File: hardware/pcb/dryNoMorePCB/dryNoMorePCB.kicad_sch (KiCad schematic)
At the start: 25 parts, among them J1 USB_A_Stacked, J10 Jack-DC, J11 Conn_01x03, J2 Conn_01x03, J3 Conn_01x03, J4 Conn_01x03, J5 USB_A_Stacked, J6 Conn_01x03, J7 Conn_01x03, J8 Conn_01x03, J9 USB_A_Stacked, M1 MNMOS, M2 MNMOS, M3 MNMOS, M4 MNMOS, M5 MNMOS, M6 MNMOS

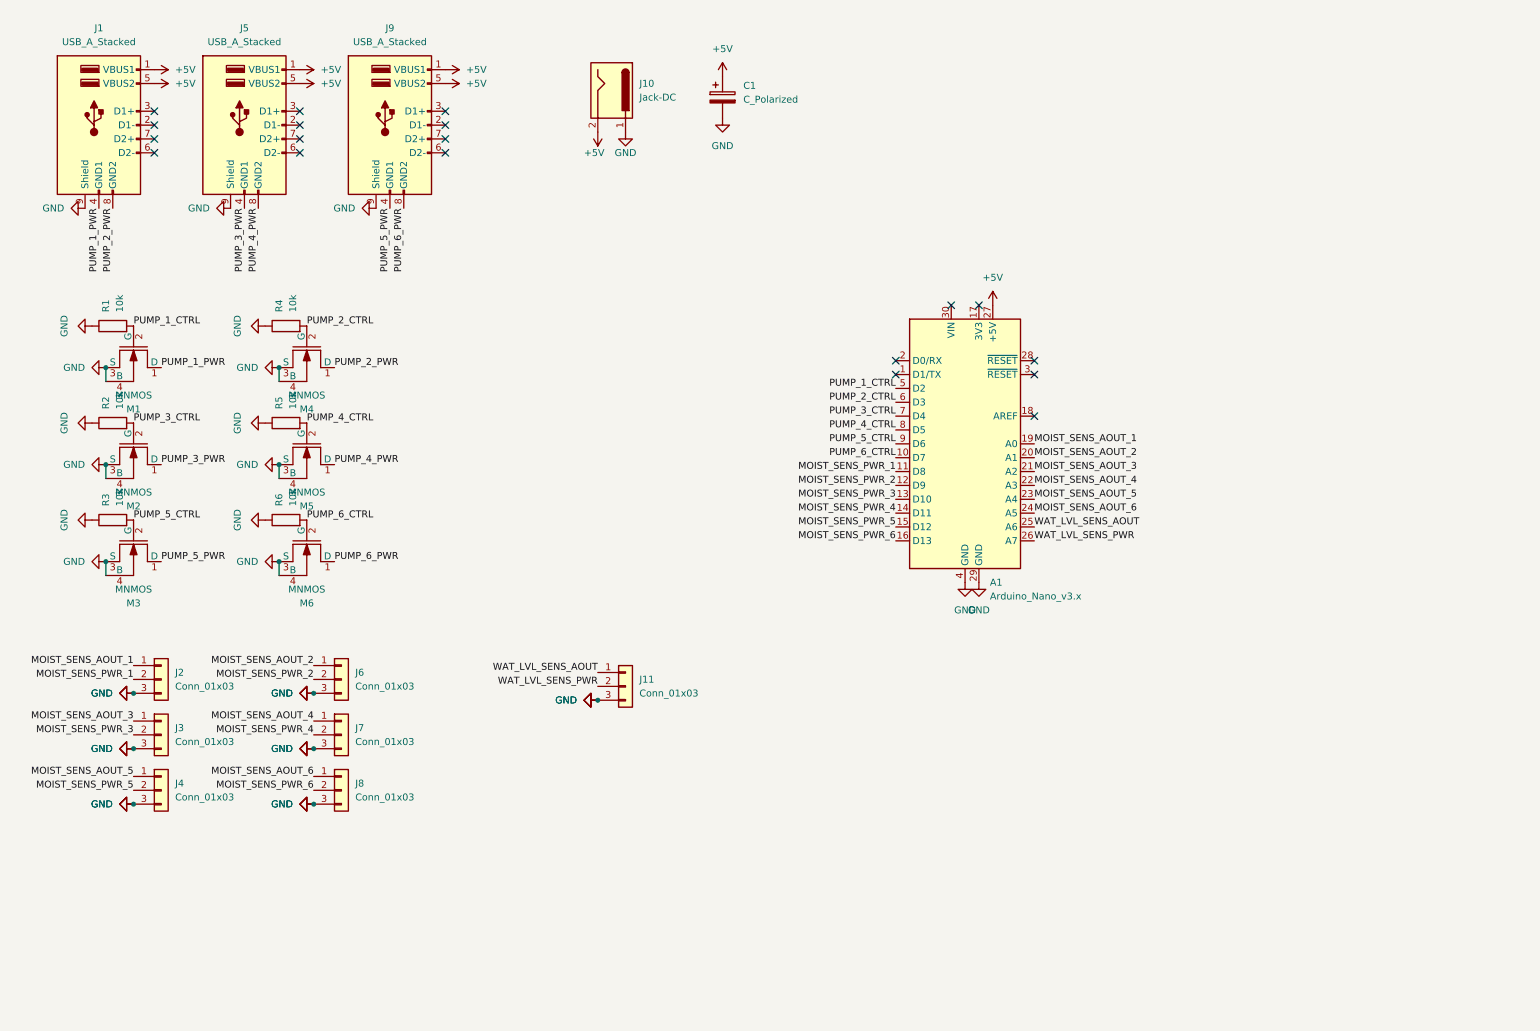
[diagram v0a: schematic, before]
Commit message: hardware: add shift register & ethernet adapter
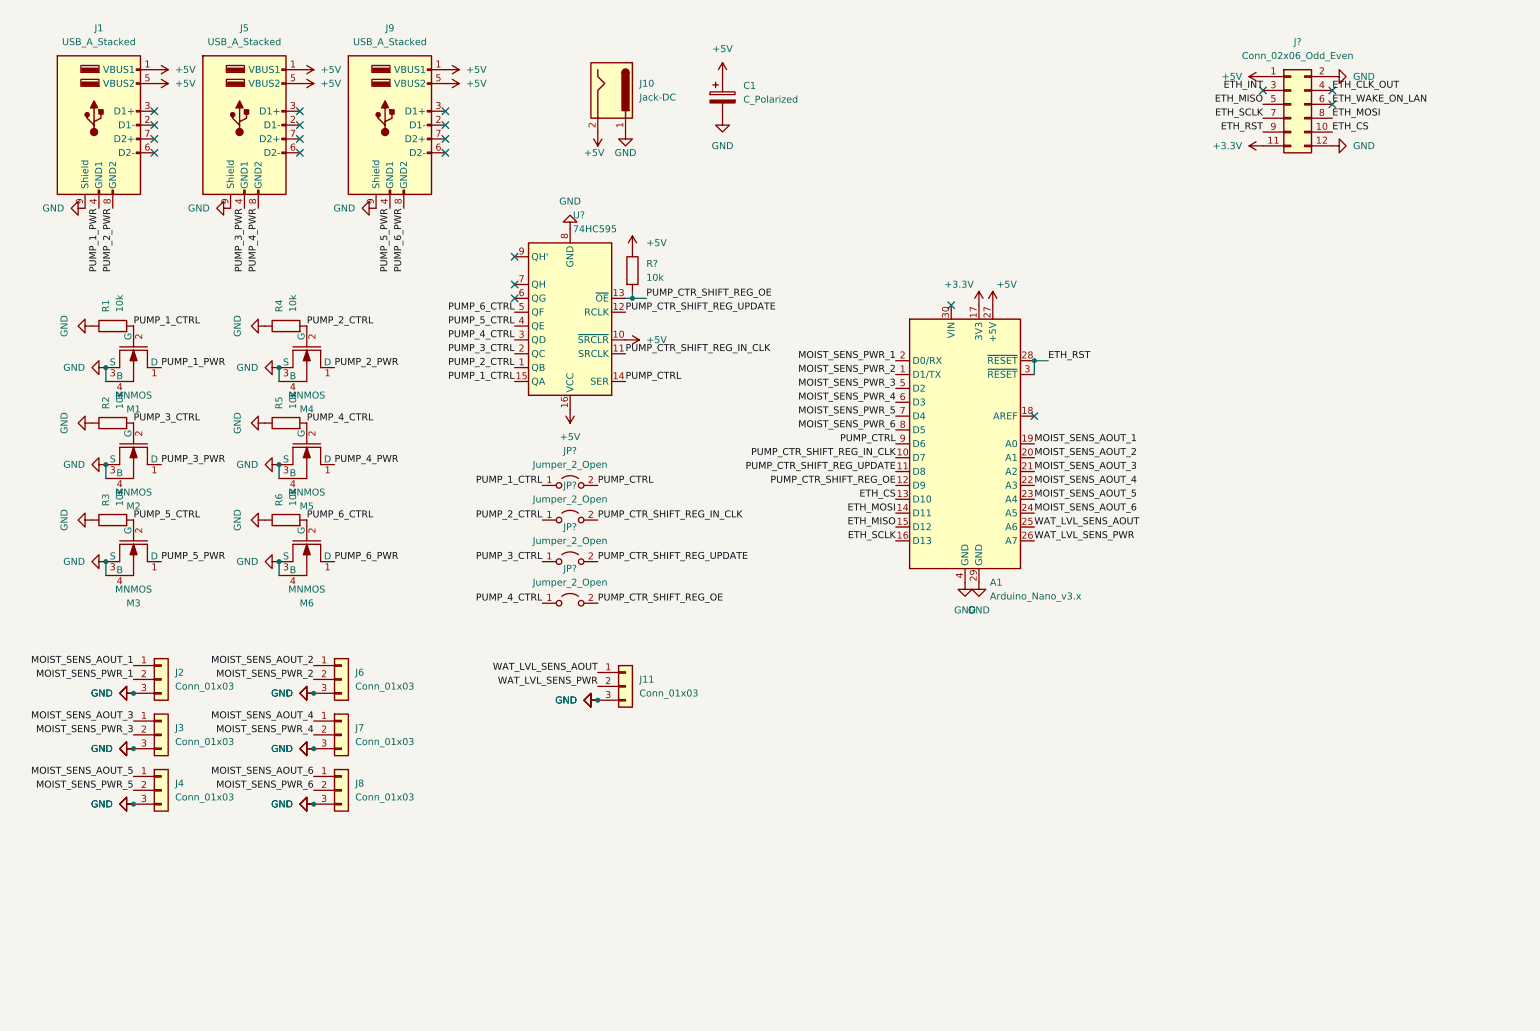
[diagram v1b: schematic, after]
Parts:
- added J?: Conn_02x06_Odd_Even, symbol Connector_Generic:Conn_02x06_Odd_Even
- added JP? (x4): Jumper_2_Open, symbol Jumper:Jumper_2_Open
- added R?: 10k, symbol Device:R
- added U?: 74HC595, symbol 74xx:74HC595
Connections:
- net +5V: now also J?.1 (Pin_1), R?.1, U?.10 (~{SRCLR}), U?.16 (VCC)
- net GND: now also J?.12 (Pin_12), J?.2 (Pin_2), U?.8 (GND)
- net MOIST_SENS_PWR_1: now also A1.2 (D0/RX); no longer A1.11 (D8)
- net MOIST_SENS_PWR_2: now also A1.1 (D1/TX); no longer A1.12 (D9)
- net MOIST_SENS_PWR_3: now also A1.5 (D2); no longer A1.13 (D10)
- net MOIST_SENS_PWR_4: now also A1.6 (D3); no longer A1.14 (D11)
- net MOIST_SENS_PWR_5: now also A1.7 (D4); no longer A1.15 (D12)
- net MOIST_SENS_PWR_6: now also A1.8 (D5); no longer A1.16 (D13)
- net PUMP_1_CTRL: now also JP?.1 (A), U?.15 (QA); no longer A1.5 (D2)
- net PUMP_2_CTRL: now also JP?.1 (A), U?.1 (QB); no longer A1.6 (D3)
- net PUMP_3_CTRL: now also JP?.1 (A), U?.2 (QC); no longer A1.7 (D4)
- net PUMP_4_CTRL: now also JP?.1 (A), U?.3 (QD); no longer A1.8 (D5)
- net PUMP_5_CTRL: now also U?.4 (QE); no longer A1.9 (D6)
- net PUMP_6_CTRL: now also U?.5 (QF); no longer A1.10 (D7)
- net +3V3: now reaches A1.17 (3V3)
- net +3V3: now also J?.11 (Pin_11)
- net ETH_RST: now reaches A1.28 (~{RESET})
- net ETH_RST: now also A1.3 (~{RESET}), J?.9 (Pin_9)
- new net ETH_CLK_OUT: J?.4 (Pin_4)
- new net ETH_CS: A1.13 (D10), J?.10 (Pin_10)
- new net ETH_INT: J?.3 (Pin_3)
- new net ETH_MISO: A1.15 (D12), J?.5 (Pin_5)
- new net ETH_MOSI: A1.14 (D11), J?.8 (Pin_8)
- new net ETH_SCLK: A1.16 (D13), J?.7 (Pin_7)
- new net ETH_WAKE_ON_LAN: J?.6 (Pin_6)
- new net PUMP_CTRL: A1.9 (D6), JP?.2 (B), U?.14 (SER)
- new net PUMP_CTR_SHIFT_REG_IN_CLK: A1.10 (D7), JP?.2 (B), U?.11 (SRCLK)
- new net PUMP_CTR_SHIFT_REG_OE: A1.12 (D9), JP?.2 (B), R?.2, U?.13 (~{OE})
- new net PUMP_CTR_SHIFT_REG_UPDATE: A1.11 (D8), JP?.2 (B), U?.12 (RCLK)
- no-connect marks 19 -> 20

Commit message: more pcb progress
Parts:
- removed J10: Jack-DC, symbol Connector:Jack-DC
- removed JP? (x4): Jumper_2_Open, symbol Jumper:Jumper_2_Open
- removed M1, M2, M3, M4, M5, M6: MNMOS, symbol pspice:MNMOS
- added C1, C4: 0.1µF, Capacitor_THT:C_Disc_D3.8mm_W2.6mm_P2.50mm, symbol Device:C_Small
- added C2, C5: 1µF, Capacitor_THT:C_Rect_L4.0mm_W2.5mm_P2.50mm, symbol Device:C_Small
- added J10: Barrel_Jack_MountingPin, Connector_BarrelJack:BarrelJack_Horizontal, symbol Connector:Barrel_Jack_MountingPin
- added J11: Conn_01x03, Connector_PinHeader_2.54mm:PinHeader_1x03_P2.54mm_Vertical, symbol Connector_Generic:Conn_01x03
- added Q1, Q2, Q3, Q4, Q5, Q6: Q_NMOS_GDSD, Package_TO_SOT_THT:TO-220-3_Vertical, symbol Device:Q_NMOS_GDSD
- added U1: 74HC595, Package_DIP:DIP-16_W7.62mm_Socket, symbol 74xx:74HC595
- C3: renamed from C1; value C_Polarized -> 470µF; footprint (none) -> Capacitor_THT:CP_Radial_D8.0mm_P3.50mm
- J13: renamed from J?; footprint (none) -> Connector_PinSocket_2.54mm:PinSocket_2x06_P2.54mm_Horizontal
- R7: renamed from R?; footprint (none) -> Resistor_THT:R_Axial_DIN0207_L6.3mm_D2.5mm_P7.62mm_Horizontal
- U2: renamed from U?; footprint (none) -> Package_DIP:DIP-16_W7.62mm_Socket
- renumbered J11 to J12
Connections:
- net +5V: now also C1.2, C2.1, C4.2, C5.1, J10.2, U1.10 (~{SRCLR}), U1.16 (VCC)
- net GND: now also C1.1, C2.2, C4.1, C5.2, J10.1, J11.3 (Pin_3), Q1.3 (S), Q2.3 (S), Q3.3 (S), Q4.3 (S), Q5.3 (S), Q6.3 (S), U1.8 (GND)
- net MOIST_SENS_PWR_1: now also U1.3 (QD); no longer A1.2 (D0/RX)
- net MOIST_SENS_PWR_2: now also U1.4 (QE); no longer A1.1 (D1/TX)
- net MOIST_SENS_PWR_3: now also U1.5 (QF); no longer A1.5 (D2)
- net MOIST_SENS_PWR_4: now also U1.6 (QG); no longer A1.6 (D3)
- net MOIST_SENS_PWR_5: now also U1.7 (QH); no longer A1.7 (D4)
- net MOIST_SENS_PWR_6: now also U1.2 (QC); no longer A1.8 (D5)
- net PUMP_1_CTRL: now also Q1.1 (G)
- net PUMP_1_PWR: now also Q1.2 (D)
- net PUMP_2_CTRL: now also Q4.1 (G)
- net PUMP_2_PWR: now also Q4.2 (D)
- net PUMP_3_CTRL: now also Q2.1 (G)
- net PUMP_3_PWR: now also Q2.2 (D)
- net PUMP_4_CTRL: now also Q5.1 (G)
- net PUMP_4_PWR: now also Q5.2 (D)
- net PUMP_5_CTRL: now also Q3.1 (G)
- net PUMP_5_PWR: now also Q3.2 (D)
- net PUMP_6_CTRL: now also Q6.1 (G)
- net PUMP_6_PWR: now also Q6.2 (D)
- net at U2.9 (QH'): now also U1.14 (SER)
- net PUMP_CTRL renamed PWR_CTRL
- net PUMP_CTR_SHIFT_REG_IN_CLK renamed PWR_CTRL_SHIFT_REG_IN_CLK
- net PWR_CTRL_SHIFT_REG_IN_CLK: now also U1.11 (SRCLK)
- net PUMP_CTR_SHIFT_REG_OE renamed PWR_CTRL_SHIFT_REG_OE
- net PWR_CTRL_SHIFT_REG_OE: now also U1.13 (~{OE})
- net PUMP_CTR_SHIFT_REG_UPDATE renamed PWR_CTRL_SHIFT_REG_UPDATE
- net PWR_CTRL_SHIFT_REG_UPDATE: now also U1.12 (RCLK)
- net WAT_LVL_SENS_AOUT renamed WAT_LVL_SENS_AOUT_1
- net WAT_LVL_SENS_AOUT_1: now also J11.1 (Pin_1); no longer J12.1 (Pin_1)
- net WAT_LVL_SENS_PWR renamed WAT_LVL_SENS_AOUT_2
- net WAT_LVL_SENS_AOUT_2: now also J12.1 (Pin_1); no longer J12.2 (Pin_2)
- new net WAT_LVL_SENS_PWR_1: J11.2 (Pin_2), U1.15 (QA)
- new net WAT_LVL_SENS_PWR_2: J12.2 (Pin_2), U1.1 (QB)
- no-connect marks 20 -> 34
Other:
- moved on the sheet: A1, J12, J2, J3, J4, J6, J7, J8, R1, R2, R3, R4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

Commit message: more routing nightmares incoming
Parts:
- added J13, J15, J16, J17: Conn_01x02, Connector_PinHeader_2.54mm:PinHeader_1x02_P2.54mm_Vertical, symbol Connector_Generic:Conn_01x02
- renumbered J13 to J14
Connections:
- net ETH_RST: no longer A1.28 (~{RESET})
- net MOIST_SENS_AOUT_1: now also A1.21 (A2); no longer A1.19 (A0)
- net MOIST_SENS_AOUT_2: now also A1.22 (A3); no longer A1.20 (A1)
- net MOIST_SENS_AOUT_3: now also A1.23 (A4); no longer A1.21 (A2)
- net MOIST_SENS_AOUT_4: now also A1.26 (A7); no longer A1.22 (A3)
- net MOIST_SENS_AOUT_5: now also A1.25 (A6); no longer A1.23 (A4)
- net MOIST_SENS_PWR_4: now also U1.2 (QC); no longer U1.6 (QG)
- net MOIST_SENS_PWR_5: now also U1.1 (QB); no longer U1.7 (QH)
- net MOIST_SENS_PWR_6: now also U1.15 (QA); no longer U1.2 (QC)
- net PUMP_1_CTRL: now also U2.7 (QH); no longer U2.15 (QA)
- net PUMP_2_CTRL: now also U2.6 (QG); no longer U2.1 (QB)
- net PUMP_3_CTRL: now also U2.5 (QF); no longer U2.2 (QC)
- net PUMP_4_CTRL: now also U2.4 (QE); no longer U2.3 (QD)
- net PUMP_5_CTRL: now also U2.3 (QD); no longer U2.4 (QE)
- net PUMP_6_CTRL: now also U2.2 (QC); no longer U2.5 (QF)
- net PWR_CTRL_SHIFT_REG_IN_CLK: now also A1.11 (D8); no longer A1.10 (D7)
- net PWR_CTRL_SHIFT_REG_UPDATE: now also A1.10 (D7); no longer A1.11 (D8)
- net WAT_LVL_SENS_AOUT_1: now also A1.20 (A1); no longer A1.25 (A6)
- net WAT_LVL_SENS_AOUT_2: now also A1.19 (A0); no longer A1.26 (A7)
- net WAT_LVL_SENS_PWR_1: now also U1.7 (QH); no longer U1.15 (QA)
- net WAT_LVL_SENS_PWR_2: now also U1.6 (QG); no longer U1.1 (QB)
- net UNUSED_D_PIN_2: now reaches A1.1 (D1/TX)
- net UNUSED_D_PIN_2: now also J15.2 (Pin_2)
- net UNUSED_D_PIN_1: now reaches A1.2 (D0/RX)
- net UNUSED_D_PIN_1: now also J15.1 (Pin_1)
- net UNUSED_D_PIN_3: now reaches A1.5 (D2)
- net UNUSED_D_PIN_3: now also J16.1 (Pin_1)
- net UNUSED_D_PIN_4: now reaches A1.6 (D3)
- net UNUSED_D_PIN_4: now also J16.2 (Pin_2)
- net UNUSED_D_PIN_5: now reaches A1.7 (D4)
- net UNUSED_D_PIN_5: now also J17.1 (Pin_1)
- net UNUSED_D_PIN_6: now reaches A1.8 (D5)
- net UNUSED_D_PIN_6: now also J17.2 (Pin_2)
- new net UNUSED_PWR_CTRL_1: J13.1 (Pin_1), U2.15 (QA)
- new net UNUSED_PWR_CTRL_2: J13.2 (Pin_2), U2.1 (QB)
- no-connect marks 34 -> 27
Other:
- moved on the sheet: C1, C2

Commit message: almost done with the pcb
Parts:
- removed J14: Conn_02x06_Odd_Even, Connector_PinSocket_2.54mm:PinSocket_2x06_P2.54mm_Horizontal, symbol Connector_Generic:Conn_02x06_Odd_Even
- added H1, H2, H3, H4: MountingHole, MountingHole:MountingHole_3.2mm_M3_DIN965, symbol Mechanical:MountingHole
- added J14: ETH_W5500, Connector_PinHeader_2.54mm:PinHeader_2x05_P2.54mm_Vertical, symbol Connector_Generic:Conn_02x05_Odd_Even
- added J18, J19: GND, Connector_PinHeader_2.54mm:PinHeader_1x02_P2.54mm_Vertical, symbol Connector_Generic:Conn_01x02
- added J20, J21: +5V, Connector_PinHeader_2.54mm:PinHeader_1x02_P2.54mm_Vertical, symbol Connector_Generic:Conn_01x02
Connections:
- net +3V3: now also J14.9 (Pin_9)
- net +5V: now also J14.10 (Pin_10), J20.1 (Pin_1), J20.2 (Pin_2), J21.1 (Pin_1), J21.2 (Pin_2)
- net ETH_CS: now also J14.3 (Pin_3)
- net ETH_INT: now also J14.4 (Pin_4)
- net ETH_MISO: now also J14.7 (Pin_7)
- net ETH_MOSI: now also J14.5 (Pin_5)
- net ETH_RST: now also A1.28 (~{RESET}), J14.6 (Pin_6); no longer A1.3 (~{RESET})
- net ETH_SCLK: now also J14.1 (Pin_1)
- net GND: now also J14.8 (Pin_8), J18.1 (Pin_1), J18.2 (Pin_2), J19.1 (Pin_1), J19.2 (Pin_2)
- net MOIST_SENS_AOUT_3: now also A1.26 (A7); no longer A1.23 (A4)
- net MOIST_SENS_AOUT_4: now also A1.23 (A4); no longer A1.26 (A7)
- net MOIST_SENS_AOUT_5: now also A1.24 (A5); no longer A1.25 (A6)
- net MOIST_SENS_AOUT_6: now also A1.25 (A6); no longer A1.24 (A5)
- net MOIST_SENS_PWR_1: now also U1.4 (QE); no longer U1.3 (QD)
- net MOIST_SENS_PWR_2: now also U1.3 (QD); no longer U1.4 (QE)
- net MOIST_SENS_PWR_3: now also U1.2 (QC); no longer U1.5 (QF)
- net MOIST_SENS_PWR_4: now also U1.6 (QG); no longer U1.2 (QC)
- net MOIST_SENS_PWR_5: now also U1.5 (QF); no longer U1.1 (QB)
- net PUMP_1_CTRL: now also U2.1 (QB); no longer U2.7 (QH)
- net PWR_CTRL: now also A1.12 (D9); no longer A1.9 (D6)
- net PWR_CTRL_SHIFT_REG_IN_CLK: now also A1.9 (D6); no longer A1.11 (D8)
- net PWR_CTRL_SHIFT_REG_OE: now also A1.11 (D8); no longer A1.12 (D9)
- net UNUSED_PWR_CTRL_2: now also U2.7 (QH); no longer U2.1 (QB)
- net WAT_LVL_SENS_AOUT_1: now also A1.19 (A0); no longer A1.20 (A1)
- net WAT_LVL_SENS_AOUT_2: now also A1.20 (A1); no longer A1.19 (A0)
- net WAT_LVL_SENS_PWR_1: now also U1.1 (QB); no longer U1.7 (QH)
- net WAT_LVL_SENS_PWR_2: now also U1.7 (QH); no longer U1.6 (QG)
- no-connect marks 27 -> 26
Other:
- title: (none) -> DryNoMorePCB by 7FM

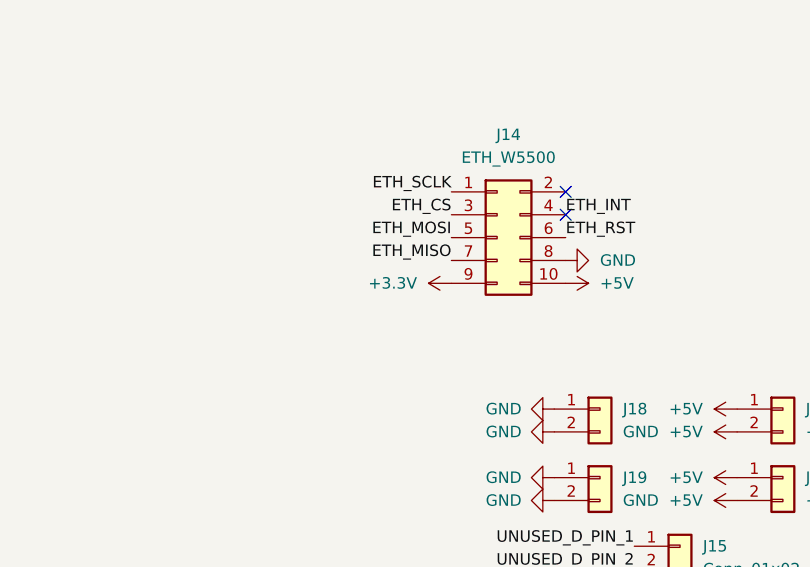
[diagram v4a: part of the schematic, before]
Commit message: eth W5500: only connect 5V, add circuit tree icon to the backside
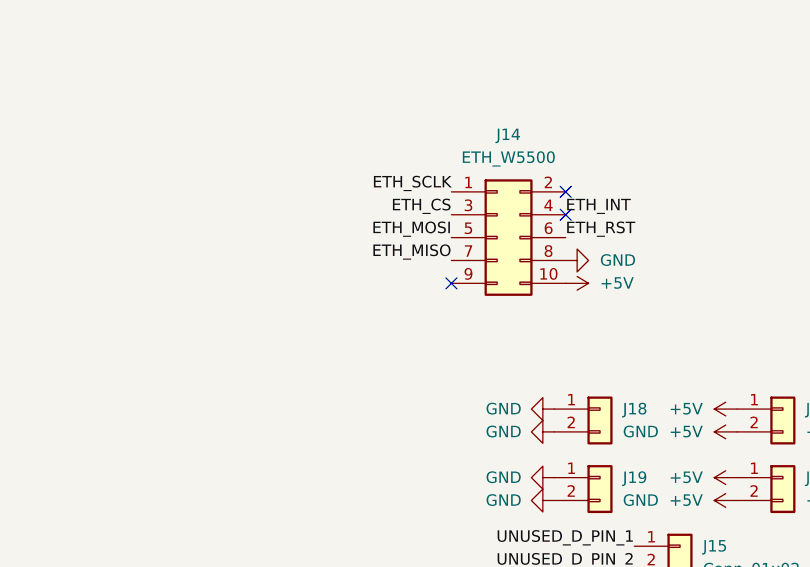
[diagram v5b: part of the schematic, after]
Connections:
- net +3V3: no longer J14.9 (Pin_9)
- no-connect marks 26 -> 27
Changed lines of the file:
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@@
   (no_connect (at 113.03 30.48))
   (no_connect (at 135.89 67.31))
+  (no_connect (at 238.76 57.15))
   (no_connect (at 247.65 107.95))
   (no_connect (at 35.56 31.75))
@@
     (pin "1")
   )
-  (symbol (lib_id "power:+3.3V") (at 238.76 57.15 90) (unit 1)
-    (in_bom yes) (on_board yes) (fields_autoplaced)
-    (property "Reference" "#PWR054" (id 0) (at 242.57 57.15 0)
-      (effects (font (size 1.27 1.27)) hide)
-    )
-    (property "Value" "+3.3V" (id 1) (at 234.95 57.1499 90)
-      (effects (font (size 1.27 1.27)) (justify left))
-    )
-    (property "Footprint" "" (id 2) (at 238.76 57.15 0)
-      (effects (font (size 1.27 1.27)) hide)
-    )
-    (property "Datasheet" "" (id 3) (at 238.76 57.15 0)
-      (effects (font (size 1.27 1.27)) hide)
-    )
-    (pin "1")
-  )
   (symbol (lib_id "Device:R") (at 163.83 110.49 0) (unit 1)
     (in_bom yes) (on_board yes) (fields_autoplaced)
@@
       (reference "#PWR053") (unit 1) (value "+5V") (footprint "")
     )
-    (path "/c3587716-c418-445e-8f42-be54608d652f"
-      (reference "#PWR054") (unit 1) (value "+3.3V") (footprint "")
-    )
     (path "/1e09c4c6-70c4-4651-a160-9a2b937de738"
